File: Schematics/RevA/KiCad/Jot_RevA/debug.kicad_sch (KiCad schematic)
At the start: 7 parts

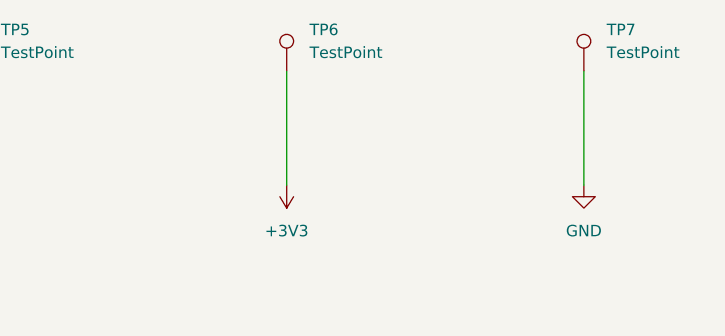
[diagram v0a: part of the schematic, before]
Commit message: Rev A schematic final: battery fuse, reverse protection, VBUS TVS, charge inhibit, 32 MB flash
Polyfuse F1 and reverse-polarity P-FET Q6 between J2 and +BATT; SMF5.0A TVS on
VBUS; firmware charge inhibit (Q7/Q8, R20/R21, CHG_INHIBIT on P1.11, charging on
by default); R19 10R 1 W 2512; I2C pull-ups 2.2k; 1k series resistor on BTN;
flash W25Q256JVEIQ (symbol renamed); TP1/TP2/TP6 and J2 labels; junction dots.
BOM, pin list and architecture draft 5 updated (section 4.14: protection summary
and known Rev A limitations). JLCPCB upload BOM added. ERC clean.
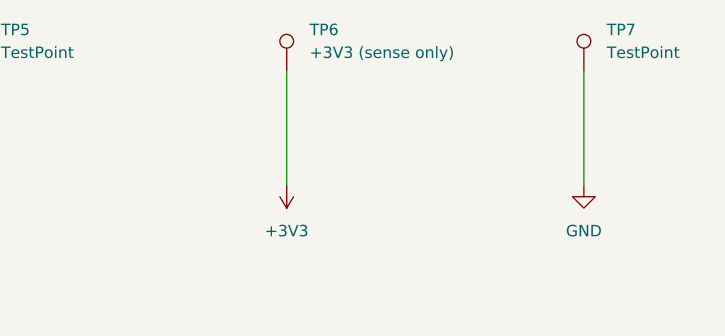
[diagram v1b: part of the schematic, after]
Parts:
- TP6: value TestPoint -> +3V3 (sense only)
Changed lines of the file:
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@@
 			)
 		)
-		(property "Value" "TestPoint"
+		(property "Value" "+3V3 (sense only)"
 			(at 189.23 53.8479 0)
 			(show_name no)
